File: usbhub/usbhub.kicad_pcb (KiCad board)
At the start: 2 copper layers, 100 x 36.5 mm, 44 parts, among them J1 USB_A, J2 USB_A, J3 USB_InputPort, J4 USB_A, J5 USB_InputPort, J6 USB_A, J7 Conn_01x05_Male, J8 Power, J9 Power, U1 FE1.1s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

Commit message: update pcb
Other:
- outline, holes or cut-outs redrawn
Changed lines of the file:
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@@
   )
   (gr_line locked (start 191.515 82.61) (end 191.515 119.06) (layer "Edge.Cuts") (width 0.1))
-  (gr_circle (center 95.015 115.56) (end 97.515 115.56) (layer "Edge.Cuts") (width 0.1) (fill none))
+  (gr_circle (center 95.015 115.56) (end 96.615 115.56) (layer "Edge.Cuts") (width 0.1) (fill none))
   (gr_line locked (start 91.515 119.06) (end 191.515 119.06) (layer "Edge.Cuts") (width 0.1))
-  (gr_circle (center 188.015 86.11) (end 190.515 86.11) (layer "Edge.Cuts") (width 0.1) (fill none))
-  (gr_circle (center 188.015 115.56) (end 190.515 115.56) (layer "Edge.Cuts") (width 0.1) (fill none))
+  (gr_circle (center 188.015 86.11) (end 189.615 86.11) (layer "Edge.Cuts") (width 0.1) (fill none))
+  (gr_circle (center 188.015 115.56) (end 189.615 115.56) (layer "Edge.Cuts") (width 0.1) (fill none))
   (gr_line locked (start 91.515 82.61) (end 91.515 119.06) (layer "Edge.Cuts") (width 0.1))
-  (gr_circle (center 95.015 86.11) (end 97.515 86.11) (layer "Edge.Cuts") (width 0.1) (fill none))
+  (gr_circle (center 95.015 86.11) (end 96.615 86.11) (layer "Edge.Cuts") (width 0.1) (fill none))
   (gr_line locked (start 91.515 82.61) (end 191.515 82.61) (layer "Edge.Cuts") (width 0.1))
   (dimension (type aligned) (layer "Cmts.User")

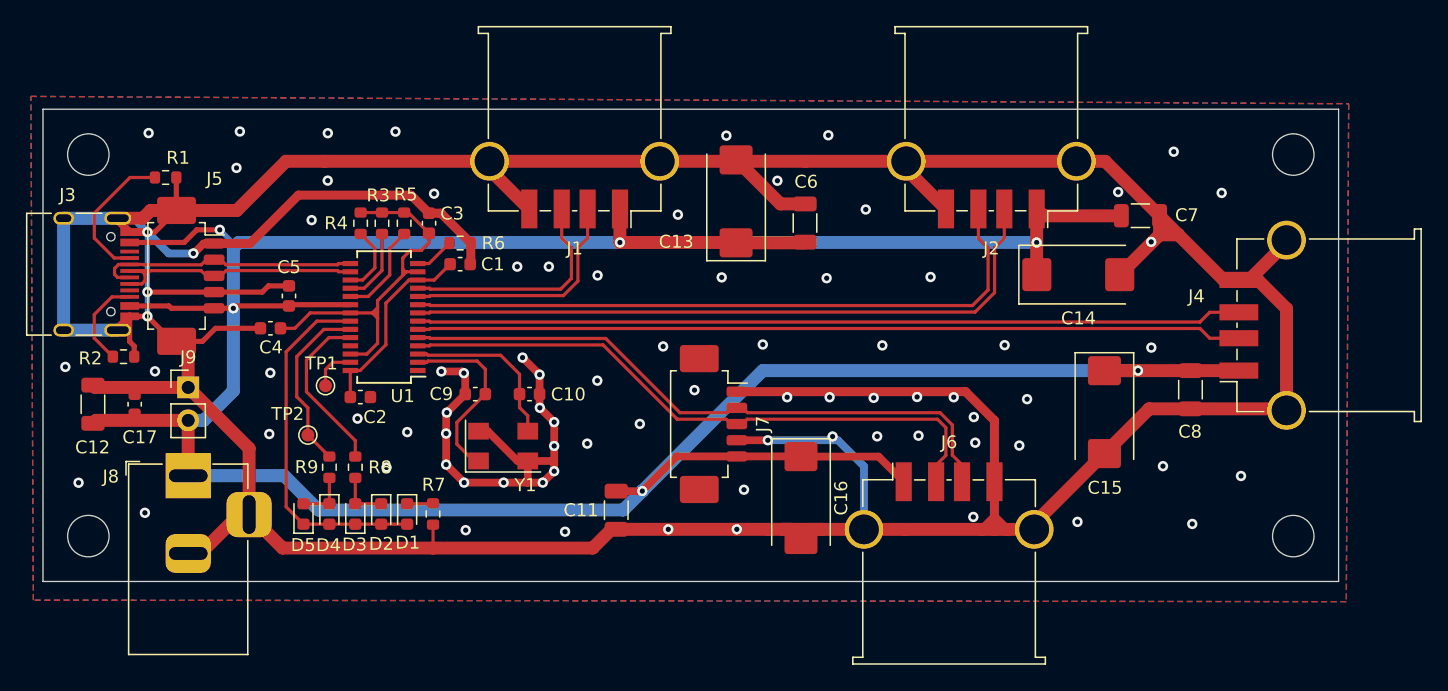
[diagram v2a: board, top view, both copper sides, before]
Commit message: change usb2.0 hub board design
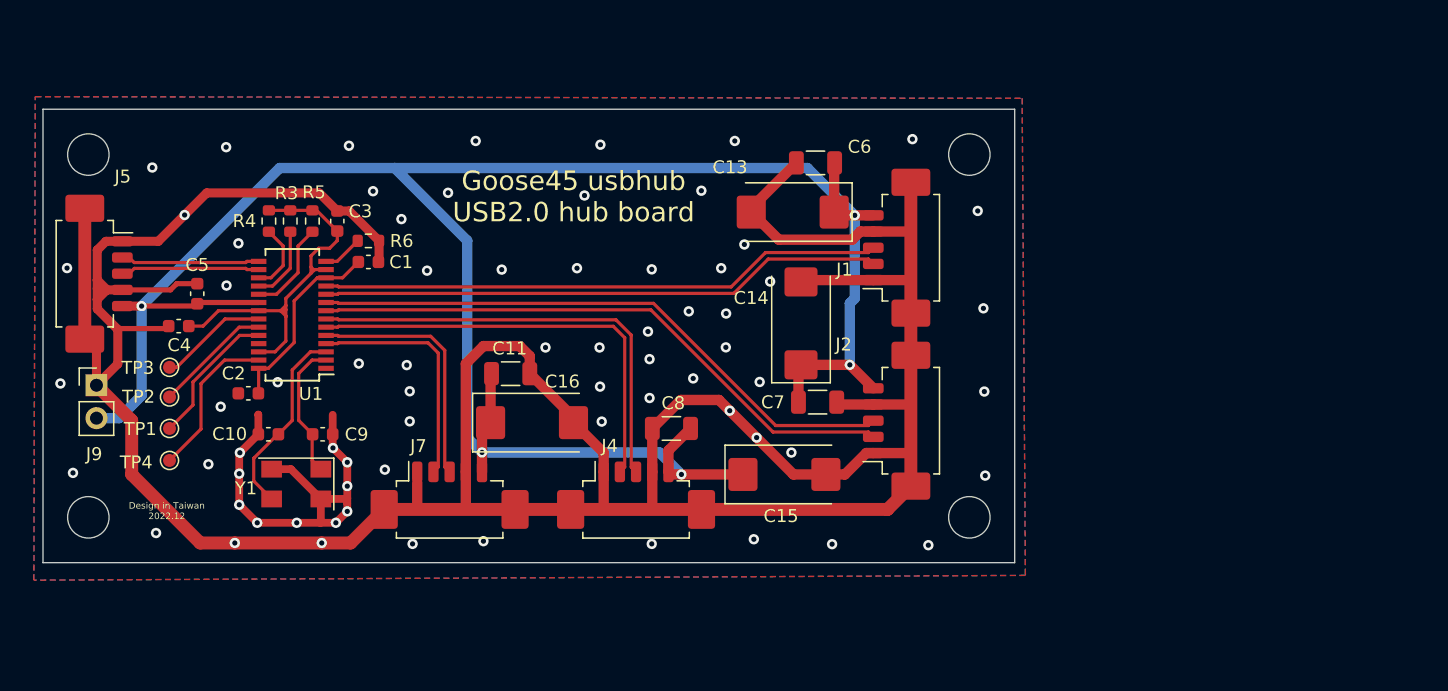
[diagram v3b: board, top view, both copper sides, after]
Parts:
- removed C12: 100uF/16V, Capacitor_SMD:C_1206_3216Metric
- removed C17: 100uF/16V, Capacitor_SMD:C_0603_1608Metric
- removed D1, D2, D3, D4, D5: LED, LED_SMD:LED_0603_1608Metric
- removed J3: USB_InputPort, Connector_USB:USB_C_Receptacle_HRO_TYPE-C-31-M-12
- removed J6: USB_A, Connector_USB:USB_A_TE_292303-7_Horizontal
- removed J8: Power, Connector_BarrelJack:BarrelJack_Horizontal
- removed R1, R2: 5.1K, Resistor_SMD:R_0603_1608Metric
- removed R7, R8, R9: 330, Resistor_SMD:R_0603_1608Metric
- added TP3: TestPoint, TestPoint:TestPoint_Pad_D1.0mm, F.Cu at (101.3, 102.5)
- added TP4: TestPoint, TestPoint:TestPoint_Pad_D1.0mm, F.Cu at (101.3, 107.2)
- J1, J2, J4: value USB_A -> Conn_01x05_Male; footprint Connector_USB:USB_A_TE_292303-7_Horizontal -> Connector_Molex:Molex_PicoBlade_53261-0571_1x05-1MP_P1.25mm_Horizontal
- moved J4 54.7 mm to (137.3, 113.0), turned to 0 degrees
- moved C8 40.2 mm to (140.0, 107.2), turned to 180 degrees
- moved C7 28.8 mm to (151.3, 105.2)
- moved J1 27.1 mm to (158.0, 93.3), turned to 90 degrees
- moved C15 25.2 mm to (148.7, 110.8), turned to 0 degrees
- moved J2 23.7 mm to (158.0, 106.7), turned to 90 degrees
- moved C14 21.7 mm to (150.0, 99.1), turned to 90 degrees
- moved C16 21.6 mm to (129.3, 106.8), turned to 0 degrees
- moved J7 20.7 mm to (122.9, 113.0), turned to 0 degrees
- moved C10 20.4 mm to (108.9, 107.7), turned to 180 degrees
- moved Y1 16.2 mm to (111.1, 111.5), turned to 180 degrees
- moved TP1 13.4 mm to (101.3, 109.7)
- moved C11 13.3 mm to (127.6, 103.0), turned to 0 degrees
- moved C9 12.2 mm to (113.1, 107.7), turned to 0 degrees
- moved TP2 11.1 mm to (101.3, 104.8)
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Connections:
- J1 pad 1: VIN -> GND
- J1 pad 5: GND -> VIN
- J2 pad 1: VIN -> GND
- J2 pad 5: GND -> VIN
- J4 pad 1: VIN -> GND
- J4 pad 5: GND -> VIN
- J7 pad 2: USB4_D+ -> USB4_D-
- J7 pad 3: USB4_D- -> USB4_D+
- J7 pad MP: (no net) -> GND
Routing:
- net GND: track 431.6 -> 291.3 mm, vias 82 -> 71
- net VIN: track 257.4 -> 169.3 mm, vias 6 -> 5
- net USB4_D+: track 49.1 -> 19.2 mm
- net USB4_D-: track 48.2 -> 18.3 mm
- net USB3_D-: track 63.7 -> 34.0 mm
- net USB3_D+: track 63.7 -> 34.8 mm
- net USB1_D+: track 17.9 -> 43.5 mm
- net USB1_D-: track 18.7 -> 43.5 mm
- net DRV: track 27.8 -> 8.43 mm
- net Net-(J3-PadA5): track 11.1 -> 0.00 mm
- net USB_D+: track 21.1 -> 10.2 mm
- net USB_D-: track 20.4 -> 10.2 mm
- net EESDA: track 3.40 -> 12.1 mm
- net Net-(J3-PadB5): track 7.14 -> 0.00 mm
- net USB2_D-: track 51.9 -> 46.3 mm
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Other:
- board size 100 x 36.5 mm -> 75 x 35 mm
- board text added: "Design in Taiwan 2022.12"
- board text added: "Goose45 usbhub USB2.0 hub board"
